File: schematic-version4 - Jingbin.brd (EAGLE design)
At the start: 47 x 28 mm, 54 parts, among them J2 FTDI_DEVICE, M1 WIRELESS-NRF24L01, Q1 NX3225GD, T1 NMOS, T2 NMOS, T3 NMOS, T4 NMOS, U1 ATMEGA328P_TQFP, U2 GY-521MPU6050

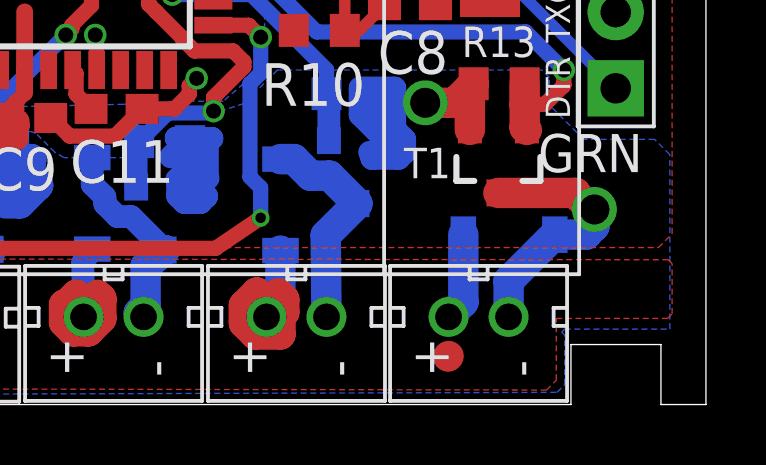
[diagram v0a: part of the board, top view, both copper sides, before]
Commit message: Removed thermal for motor 4
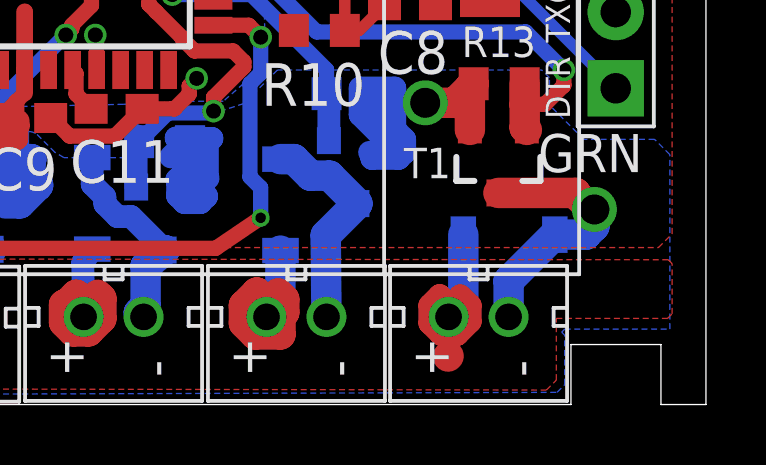
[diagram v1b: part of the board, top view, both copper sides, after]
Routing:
- net PWR: track 61.8 -> 66.4 mm
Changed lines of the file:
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@@
 <wire x1="20.1328" y1="5.6736" x2="20.1582" y2="2.8956" width="0.762" layer="16"/>
 <wire x1="19.9644" y1="5.842" x2="20.1328" y2="5.6736" width="0.762" layer="16"/>
-<polygon width="0.1524" layer="1">
+<polygon width="0.1524" layer="1" thermals="no">
 <vertex x="41.6814" y="0.4826"/>
 <vertex x="42.0116" y="0.8128"/>
@@
 <wire x1="6.858" y1="11.0236" x2="6.858" y2="10.2743" width="0.381" layer="1"/>
 <wire x1="6.858" y1="10.2743" x2="6.5659" y2="9.9822" width="0.381" layer="1"/>
+<wire x1="38.4208" y1="2.921" x2="38.4208" y2="3.3368" width="0.762" layer="1"/>
+<wire x1="38.4208" y1="3.3368" x2="38.1254" y2="3.6322" width="0.762" layer="1"/>
+<wire x1="38.1254" y1="3.6322" x2="37.7952" y2="3.302" width="0.762" layer="1"/>
+<wire x1="37.7952" y1="2.7178" x2="38.1762" y2="2.3368" width="0.762" layer="1"/>
+<wire x1="38.1762" y1="2.3368" x2="38.7096" y2="2.3368" width="0.762" layer="1"/>
+<wire x1="39.1414" y1="3.302" x2="38.8112" y2="3.6322" width="0.762" layer="1"/>
+<wire x1="37.7952" y1="3.302" x2="37.7952" y2="2.7178" width="0.762" layer="1"/>
+<wire x1="38.7096" y1="2.3368" x2="39.1414" y2="2.7686" width="0.762" layer="1"/>
+<wire x1="39.1414" y1="2.7686" x2="39.1414" y2="3.302" width="0.762" layer="1"/>
 </signal>
 <signal name="N$8">

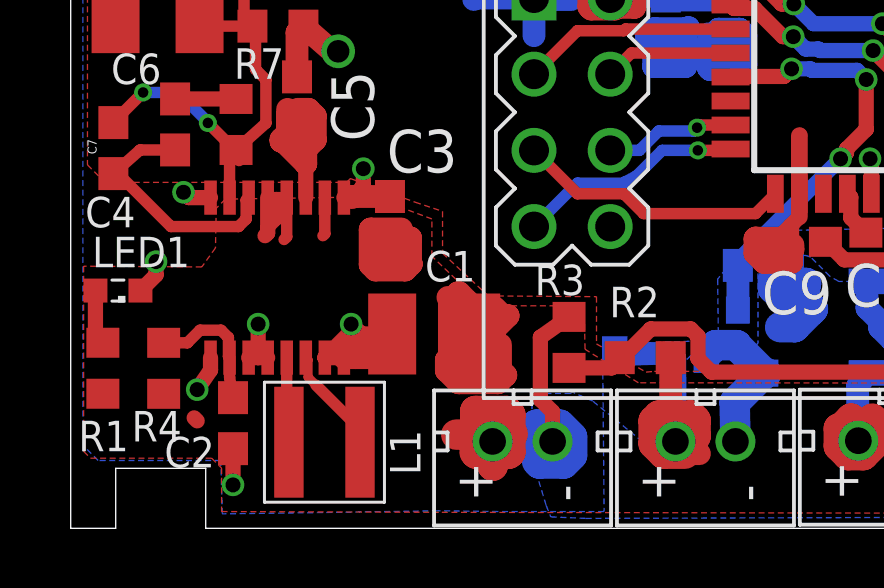
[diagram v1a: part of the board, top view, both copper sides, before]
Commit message: Change 100uF capacitor size
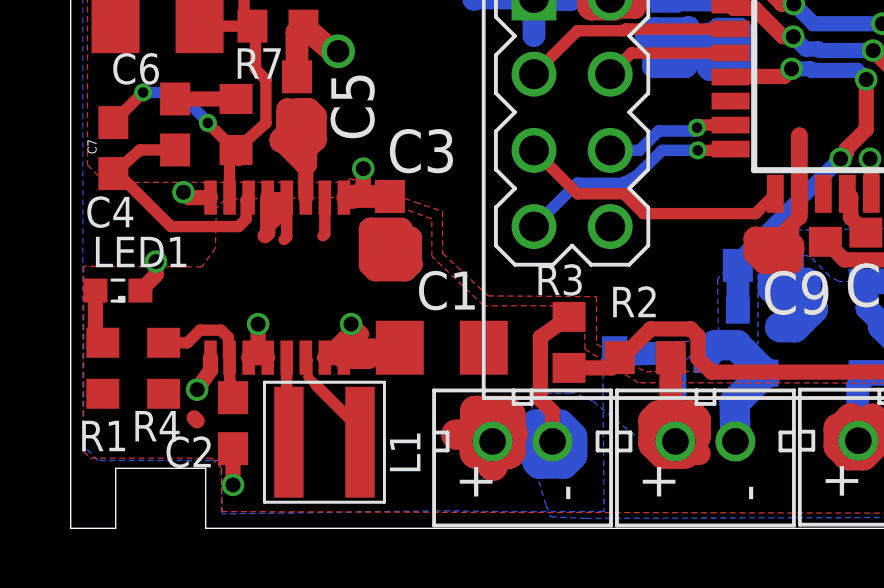
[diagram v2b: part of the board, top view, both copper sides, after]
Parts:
- C1: device rcl:C1210 -> rcl:C1206
- moved C1 0.52 mm to (12.4, 6.02)
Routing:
- net PWR: track 66.4 -> 55.8 mm
- net GND: track 115.5 -> 113.7 mm
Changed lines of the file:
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@@
 </autorouter>
 <elements>
-<element name="C1" library="rcl" library_urn="urn:adsk.eagle:library:334" package="C1210" package3d_urn="urn:adsk.eagle:package:23619/2" value="100uF" x="12.1158" y="6.477" smashed="yes" rot="R180">
-<attribute name="NAME" x="13.4874" y="9.2456" size="1.016" layer="25" rot="R180"/>
-<attribute name="SPICEPREFIX" value="C" x="12.1158" y="6.477" size="1.778" layer="27" rot="R180" display="off"/>
-</element>
 <element name="C10" library="rcl" library_urn="urn:adsk.eagle:library:334" package="C0603" package3d_urn="urn:adsk.eagle:package:23616/2" value="0.1uF" x="26.9494" y="21.8694" smashed="yes">
 <attribute name="NAME" x="27.1272" y="22.86" size="1.016" layer="25" rot="R90"/>
@@
 <element name="U2" library="quad" package="GY-521" value="GY-521MPU6050" x="15.6718" y="15.7988" smashed="yes" rot="MR270"/>
 <element name="Q1" library="NDK" package="NX3225GD-CRA-3" value="NX3225GD" x="20.0914" y="21.0566" smashed="yes" rot="R90"/>
+<element name="C1" library="rcl" library_urn="urn:adsk.eagle:library:334" package="C1206" package3d_urn="urn:adsk.eagle:package:23618/2" value="100uF" x="12.3698" y="6.0198" smashed="yes" rot="R180">
+<attribute name="NAME" x="13.6144" y="8.5598" size="1.27" layer="25" rot="R180"/>
+<attribute name="SPICEPREFIX" value="C" x="12.3698" y="6.0198" size="1.778" layer="27" rot="R180" display="off"/>
+</element>
 </elements>
 <signals>
@@
 <contactref element="J2" pad="P$5"/>
 <contactref element="U2" pad="GND"/>
-<contactref element="C1" pad="2"/>
 <contactref element="M1" pad="1"/>
 <contactref element="U$1" pad="-"/>
@@
 <wire x1="9.1059" y1="5.6896" x2="9.4996" y2="5.6896" width="0.762" layer="1"/>
 <wire x1="9.4996" y1="5.6896" x2="9.9284" y2="5.6896" width="0.762" layer="1"/>
-<wire x1="9.9284" y1="5.6896" x2="10.7158" y2="6.477" width="0.762" layer="1"/>
 <wire x1="6.2484" y1="5.6896" x2="6.2484" y2="6.8072" width="0.508" layer="1"/>
 <via x="6.2484" y="6.8072" extent="1-16" drill="0.5"/>
-<wire x1="10.7158" y1="6.477" x2="9.7028" y2="6.477" width="0.508" layer="1"/>
 <wire x1="9.7028" y1="6.477" x2="9.3472" y2="6.8072" width="0.508" layer="1"/>
 <via x="9.3472" y="6.8072" extent="1-16" drill="0.5"/>
@@
 <wire x1="9.4996" y1="6.6802" x2="9.4996" y2="6.0706" width="0.508" layer="1"/>
 <wire x1="9.4996" y1="6.0706" x2="9.4996" y2="5.6896" width="0.508" layer="1"/>
-<wire x1="10.7158" y1="6.477" x2="10.3094" y2="6.0706" width="0.508" layer="1"/>
-<wire x1="10.3094" y1="6.0706" x2="9.4996" y2="6.0706" width="0.508" layer="1"/>
+<wire x1="10.3094" y1="6.0706" x2="10.033" y2="6.0706" width="0.508" layer="1"/>
+<wire x1="10.033" y1="6.0706" x2="9.4996" y2="6.0706" width="0.508" layer="1"/>
 <wire x1="9.3726" y1="11.0236" x2="9.1059" y2="11.0236" width="0.508" layer="1"/>
 <wire x1="10.6426" y1="11.0608" x2="9.4098" y2="11.0608" width="0.762" layer="1"/>
@@
 <wire x1="27.57086875" y1="21.337" x2="27.5144" y2="21.28053125" width="0.5588" layer="1"/>
 <wire x1="27.57086875" y1="21.64086875" x2="27.57086875" y2="21.337" width="0.5588" layer="1"/>
+<contactref element="C1" pad="2"/>
+<wire x1="10.9698" y1="6.0198" x2="10.0838" y2="6.0198" width="0.1524" layer="1"/>
+<wire x1="10.0838" y1="6.0198" x2="10.033" y2="6.0706" width="0.1524" layer="1"/>
 </signal>
 <signal name="SDA">
@@
 <signal name="PWR">
 <contactref element="U$1" pad="+"/>
-<contactref element="C1" pad="1"/>
 <contactref element="R2" pad="2"/>
 <contactref element="U$4" pad="+"/>
@@
 <wire x1="8.4709" y1="11.0236" x2="8.4709" y2="9.8171" width="0.381" layer="1"/>
 <wire x1="8.4709" y1="9.8171" x2="8.4074" y2="9.7536" width="0.381" layer="1"/>
-<wire x1="13.5158" y1="6.477" x2="13.97" y2="6.477" width="0.762" layer="1"/>
-<wire x1="13.97" y1="6.477" x2="14.5796" y2="7.0866" width="0.762" layer="1"/>
-<wire x1="14.5796" y1="7.0866" x2="14.4018" y2="7.0866" width="0.762" layer="1"/>
-<wire x1="14.4018" y1="7.0866" x2="14.1224" y2="7.366" width="0.762" layer="1"/>
-<wire x1="13.5158" y1="6.477" x2="12.9032" y2="7.0896" width="0.762" layer="1"/>
-<wire x1="12.9032" y1="7.0896" x2="12.9032" y2="7.8486" width="0.762" layer="1"/>
-<wire x1="12.9032" y1="7.8486" x2="12.954" y2="7.8486" width="0.762" layer="1"/>
-<wire x1="12.954" y1="7.8486" x2="13.2588" y2="7.5438" width="0.762" layer="1"/>
-<wire x1="13.2588" y1="7.5438" x2="12.7254" y2="7.5438" width="0.762" layer="1"/>
-<wire x1="12.7254" y1="7.5438" x2="12.6238" y2="7.6454" width="0.762" layer="1"/>
-<wire x1="12.573" y1="7.6962" x2="12.6238" y2="7.6454" width="0.762" layer="1"/>
-<wire x1="12.6238" y1="5.715" x2="12.5222" y2="5.6134" width="0.762" layer="1"/>
-<wire x1="12.5222" y1="5.6134" x2="12.5222" y2="5.2578" width="0.762" layer="1"/>
-<wire x1="14.2494" y1="4.8514" x2="14.5034" y2="5.1054" width="0.762" layer="1"/>
-<wire x1="14.5034" y1="5.1054" x2="14.3256" y2="5.2832" width="0.762" layer="1"/>
-<wire x1="14.3256" y1="5.2832" x2="14.3256" y2="6.1214" width="0.762" layer="1"/>
-<wire x1="12.6238" y1="7.6454" x2="12.6238" y2="5.715" width="0.762" layer="1"/>
-<wire x1="12.5222" y1="5.2578" x2="12.9286" y2="4.8514" width="0.762" layer="1"/>
-<wire x1="12.9286" y1="4.8514" x2="14.2494" y2="4.8514" width="0.762" layer="1"/>
 <wire x1="10.6426" y1="9.3608" x2="10.9592" y2="9.6774" width="0.762" layer="1"/>
 <wire x1="10.9592" y1="9.6774" x2="11.3284" y2="9.6774" width="0.762" layer="1"/>
@@
 <wire x1="38.7096" y1="2.3368" x2="39.1414" y2="2.7686" width="0.762" layer="1"/>
 <wire x1="39.1414" y1="2.7686" x2="39.1414" y2="3.302" width="0.762" layer="1"/>
+<contactref element="C1" pad="1"/>
 </signal>
 <signal name="N$8">
